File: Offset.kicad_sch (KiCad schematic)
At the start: 19 parts, among them J1 Conn_01x02, J2 Conn_01x02, J3 Conn_01x02, U1 LM358

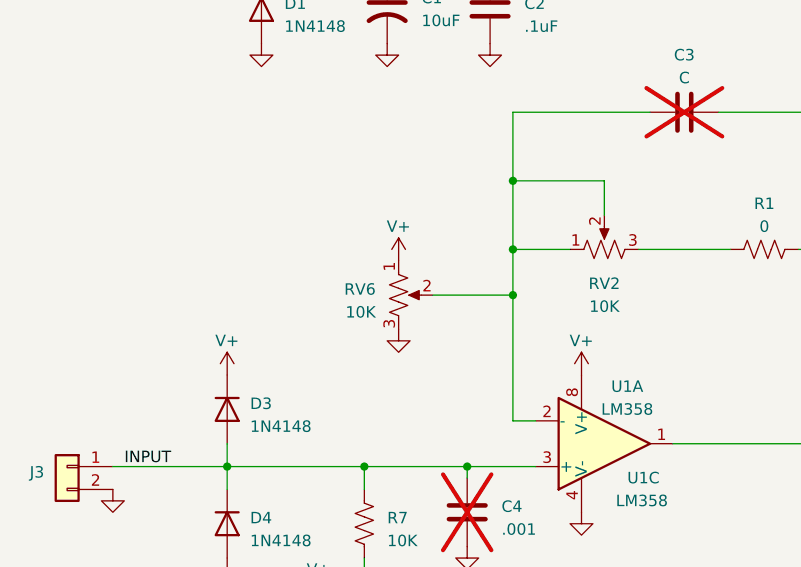
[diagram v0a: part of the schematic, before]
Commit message: Add resistor on trimmer wiper
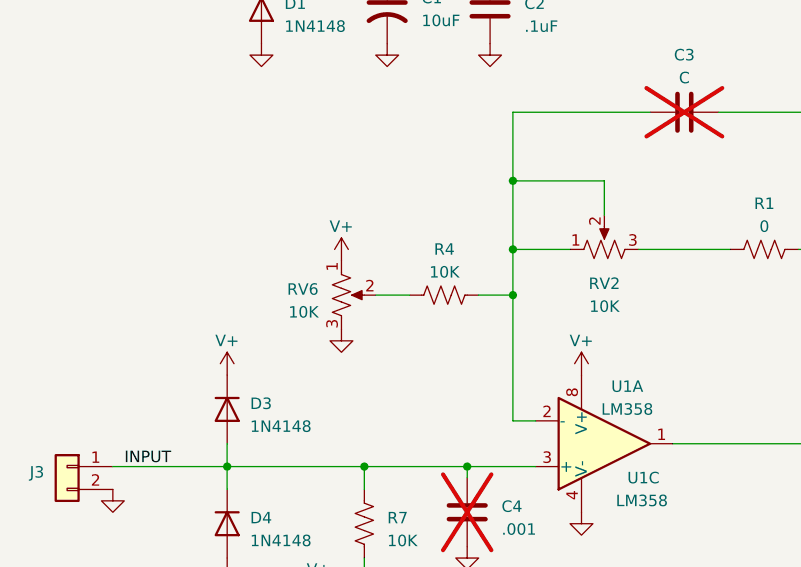
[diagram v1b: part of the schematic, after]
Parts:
- added R4: 10K, symbol Device:R_US
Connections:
- net at C3.1, RV2.1, RV2.2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: now also R4.2; no longer RV6.2
- new net: R4.1, RV6.2
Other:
- moved on the sheet: RV6
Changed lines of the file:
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@@
     (stroke (width 0) (type default))
   )
-  (wire (pts (xy 133.35 88.9) (xy 142.24 88.9))
+  (wire (pts (xy 127 88.9) (xy 130.81 88.9))
     (stroke (width 0) (type default))
   )
@@
   )
   (wire (pts (xy 156.21 83.82) (xy 166.37 83.82))
+    (stroke (width 0) (type default))
+  )
+  (wire (pts (xy 138.43 88.9) (xy 142.24 88.9))
     (stroke (width 0) (type default))
   )
@@
     )
   )
+  (symbol (lib_id "Device:R_US") (at 134.62 88.9 90) (unit 1)
+    (in_bom yes) (on_board yes) (dnp no) (fields_autoplaced)
+    (property "Reference" "R4" (at 134.62 83.82 90)
+      (effects (font (size 1.27 1.27)))
+    )
+    (property "Value" "10K" (at 134.62 86.36 90)
+      (effects (font (size 1.27 1.27)))
+    )
+    (property "Footprint" "" (at 134.874 87.884 90)
+      (effects (font (size 1.27 1.27)) hide)
+    )
+    (property "Datasheet" "~" (at 134.62 88.9 0)
+      (effects (font (size 1.27 1.27)) hide)
+    )
+    (pin "1")
+    (pin "2")
+    (instances
+      (project "Offset"
+        (path "/b9c335b0-b204-4837-ad88-f803b4ac701f"
+          (reference "R4") (unit 1)
+        )
+      )
+    )
+  )
   (symbol (lib_id "Connector_Generic:Conn_01x02") (at 198.12 105.41 0) (unit 1)
     (in_bom yes) (on_board yes) (dnp no) (fields_autoplaced)
@@
     )
   )
-  (symbol (lib_id "power:VCC") (at 129.54 85.09 0) (unit 1)
-    (in_bom yes) (on_board yes) (dnp no) (fields_autoplaced)
-    (property "Reference" "#PWR016" (at 129.54 88.9 0)
-      (effects (font (size 1.27 1.27)) hide)
-    )
-    (property "Value" "V+" (at 129.54 81.28 0)
-      (effects (font (size 1.27 1.27)))
-    )
-    (property "Footprint" "" (at 129.54 85.09 0)
-      (effects (font (size 1.27 1.27)) hide)
-    )
-    (property "Datasheet" "" (at 129.54 85.09 0)
+  (symbol (lib_id "power:VCC") (at 123.19 85.09 0) (unit 1)
+    (in_bom yes) (on_board yes) (dnp no) (fields_autoplaced)
+    (property "Reference" "#PWR016" (at 123.19 88.9 0)
+      (effects (font (size 1.27 1.27)) hide)
+    )
+    (property "Value" "V+" (at 123.19 81.28 0)
+      (effects (font (size 1.27 1.27)))
+    )
+    (property "Footprint" "" (at 123.19 85.09 0)
+      (effects (font (size 1.27 1.27)) hide)
+    )
+    (property "Datasheet" "" (at 123.19 85.09 0)
       (effects (font (size 1.27 1.27)) hide)
     )
@@
     )
   )
-  (symbol (lib_id "Device:R_Potentiometer_US") (at 129.54 88.9 0) (unit 1)
-    (in_bom yes) (on_board yes) (dnp no) (fields_autoplaced)
-    (property "Reference" "RV6" (at 127 88.265 0)
+  (symbol (lib_id "Device:R_Potentiometer_US") (at 123.19 88.9 0) (unit 1)
+    (in_bom yes) (on_board yes) (dnp no) (fields_autoplaced)
+    (property "Reference" "RV6" (at 120.65 88.265 0)
       (effects (font (size 1.27 1.27)) (justify right))
     )
-    (property "Value" "10K" (at 127 90.805 0)
+    (property "Value" "10K" (at 120.65 90.805 0)
       (effects (font (size 1.27 1.27)) (justify right))
     )
-    (property "Footprint" "" (at 129.54 88.9 0)
-      (effects (font (size 1.27 1.27)) hide)
-    )
-    (property "Datasheet" "~" (at 129.54 88.9 0)
-      (effects (font (size 1.27 1.27)) hide)
-    )
-    (property "Sim.Device" "SPICE" (at 129.54 88.9 0)
-      (effects (font (size 1.27 1.27)) hide)
-    )
-    (property "Sim.Params" "type=\"X\" model=\"RPOT value=10K ratio=0.5\" lib=RPOT_subckt.lib" (at 129.54 88.9 0)
+    (property "Footprint" "" (at 123.19 88.9 0)
+      (effects (font (size 1.27 1.27)) hide)
+    )
+    (property "Datasheet" "~" (at 123.19 88.9 0)
+      (effects (font (size 1.27 1.27)) hide)
+    )
+    (property "Sim.Device" "SPICE" (at 123.19 88.9 0)
+      (effects (font (size 1.27 1.27)) hide)
+    )
+    (property "Sim.Params" "type=\"X\" model=\"RPOT value=10K ratio=0.6\" lib=RPOT_subckt.lib" (at 123.19 88.9 0)
       (effects (font (size 1.27 1.27)) hide)
     )
@@
     )
   )
-  (symbol (lib_id "power:GND") (at 129.54 92.71 0) (unit 1)
-    (in_bom yes) (on_board yes) (dnp no) (fields_autoplaced)
-    (property "Reference" "#PWR017" (at 129.54 99.06 0)
-      (effects (font (size 1.27 1.27)) hide)
-    )
-    (property "Value" "GND" (at 129.54 97.79 0)
-      (effects (font (size 1.27 1.27)) hide)
-    )
-    (property "Footprint" "" (at 129.54 92.71 0)
-      (effects (font (size 1.27 1.27)) hide)
-    )
-    (property "Datasheet" "" (at 129.54 92.71 0)
-      (effects (font (size 1.27 1.27)) hide)
-    )
+  (symbol (lib_id "power:GND") (at 123.19 92.71 0) (unit 1)
+    (in_bom yes) (on_board yes) (dnp no) (fields_autoplaced)
+    (property "Reference" "#PWR017" (at 123.19 99.06 0)
+      (effects (font (size 1.27 1.27)) hide)
+    )
+    (property "Value" "GND" (at 123.19 97.79 0)
+      (effects (font (size 1.27 1.27)) hide)
+    )
+    (property "Footprint" "" (at 123.19 92.71 0)
+      (effects (font (size 1.27 1.27)) hide)
+    )
+    (property "Datasheet" "" (at 123.19 92.71 0)
+      (effects (font (size 1.27 1.27)) hide)
+    )

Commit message: Tweak values
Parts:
- removed RV8: 10K, symbol Device:R_Potentiometer_US
- added V2: 0.04, symbol Simulation_SPICE:VDC
- V1: value 15 -> 5
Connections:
- net GND: now also V2.2
- net at R7.1: now also V2.1
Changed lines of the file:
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@@
-    (stroke (width 0) (type default))
-  )
-  (wire (pts (xy 130.81 124.46) (xy 130.81 125.73))
-    (stroke (width 0) (type default))
-  )
-  (wire (pts (xy 129.54 124.46) (xy 130.81 124.46))
     (stroke (width 0) (type default))
   )
@@
     (stroke (width 0) (type default))
   )
-  (wire (pts (xy 125.73 118.11) (xy 125.73 120.65))
+  (wire (pts (xy 125.73 118.11) (xy 125.73 121.92))
     (stroke (width 0) (type default))
   )
@@
     (stroke (width 0) (type default))
   )
-  (wire (pts (xy 120.65 124.46) (xy 120.65 123.19))
-    (stroke (width 0) (type default))
-  )
   (wire (pts (xy 152.4 76.2) (xy 152.4 80.01))
     (stroke (width 0) (type default))
@@
   )
   (wire (pts (xy 110.49 105.41) (xy 110.49 107.95))
-    (stroke (width 0) (type default))
-  )
-  (wire (pts (xy 121.92 124.46) (xy 120.65 124.46))
     (stroke (width 0) (type default))
   )
@@
       (effects (font (size 1.27 1.27)) hide)
     )
-    (property "Sim.Params" "type=\"X\" model=\"RPOT value=10K ratio=0.6\" lib=RPOT_subckt.lib" (at 123.19 88.9 0)
+    (property "Sim.Params" "type=\"X\" model=\"RPOT value=10K ratio=0.9\" lib=RPOT_subckt.lib" (at 123.19 88.9 0)
       (effects (font (size 1.27 1.27)) hide)
     )
@@
     )
   )
-  (symbol (lib_id "Device:R_Potentiometer_US") (at 125.73 124.46 90) (unit 1)
-    (in_bom yes) (on_board yes) (dnp no) (fields_autoplaced)
-    (property "Reference" "RV8" (at 125.73 128.27 90)
-      (effects (font (size 1.27 1.27)))
-    )
-    (property "Value" "10K" (at 125.73 130.81 90)
-      (effects (font (size 1.27 1.27)))
-    )
-    (property "Footprint" "" (at 125.73 124.46 0)
-      (effects (font (size 1.27 1.27)) hide)
-    )
-    (property "Datasheet" "~" (at 125.73 124.46 0)
-      (effects (font (size 1.27 1.27)) hide)
-    )
-    (property "Sim.Device" "SPICE" (at 125.73 124.46 0)
-      (effects (font (size 1.27 1.27)) hide)
-    )
-    (property "Sim.Params" "type=\"X\" model=\"RPOT value=10K ratio=0.5\" lib=RPOT_subckt.lib" (at 125.73 124.46 0)
-      (effects (font (size 1.27 1.27)) hide)
-    )
-    (pin "1")
-    (pin "2")
-    (pin "3")
-    (instances
-      (project "Offset"
-        (path "/b9c335b0-b204-4837-ad88-f803b4ac701f"
-          (reference "RV8") (unit 1)
-        )
-      )
-    )
-  )
   (symbol (lib_id "power:GND") (at 110.49 118.11 0) (unit 1)
     (in_bom yes) (on_board yes) (dnp no) (fields_autoplaced)
@@
     )
   )
-  (symbol (lib_id "power:VCC") (at 120.65 123.19 0) (unit 1)
-    (in_bom yes) (on_board yes) (dnp no) (fields_autoplaced)
-    (property "Reference" "#PWR011" (at 120.65 127 0)
-      (effects (font (size 1.27 1.27)) hide)
-    )
-    (property "Value" "V+" (at 120.65 119.38 0)
-      (effects (font (size 1.27 1.27)))
-    )
-    (property "Footprint" "" (at 120.65 123.19 0)
-      (effects (font (size 1.27 1.27)) hide)
-    )
-    (property "Datasheet" "" (at 120.65 123.19 0)
-      (effects (font (size 1.27 1.27)) hide)
-    )
-    (pin "1")
-    (instances
-      (project "Offset"
-        (path "/b9c335b0-b204-4837-ad88-f803b4ac701f"
-          (reference "#PWR011") (unit 1)
-        )
-      )
-    )
-  )
   (symbol (lib_id "Device:C_Polarized_US") (at 128.27 57.15 0) (unit 1)
     (in_bom yes) (on_board yes) (dnp no) (fields_autoplaced)
@@
         (path "/b9c335b0-b204-4837-ad88-f803b4ac701f"
           (reference "#PWR018") (unit 1)
+        )
+      )
+    )
+  )
+  (symbol (lib_id "Simulation_SPICE:VDC") (at 125.73 127 0) (unit 1)
+    (in_bom yes) (on_board yes) (dnp no) (fields_autoplaced)
+    (property "Reference" "V2" (at 129.54 126.3292 0)
+      (effects (font (size 1.27 1.27)) (justify left))
+    )
+    (property "Value" "0.04" (at 129.54 128.8692 0)
+      (effects (font (size 1.27 1.27)) (justify left))
+    )
+    (property "Footprint" "" (at 125.73 127 0)
+      (effects (font (size 1.27 1.27)) hide)
+    )
+    (property "Datasheet" "~" (at 125.73 127 0)
+      (effects (font (size 1.27 1.27)) hide)
+    )
+    (property "Sim.Pins" "1=+ 2=-" (at 125.73 127 0)
+      (effects (font (size 1.27 1.27)) hide)
+    )
+    (property "Sim.Type" "DC" (at 125.73 127 0)
+      (effects (font (size 1.27 1.27)) hide)
+    )
+    (property "Sim.Device" "V" (at 125.73 127 0)
+      (effects (font (size 1.27 1.27)) (justify left) hide)
+    )
+    (pin "1")
+    (pin "2")
+    (instances
+      (project "Offset"
+        (path "/b9c335b0-b204-4837-ad88-f803b4ac701f"
+          (reference "V2") (unit 1)
         )
       )
@@
     )
   )
-  (symbol (lib_id "power:GND") (at 130.81 125.73 0) (unit 1)
-    (in_bom yes) (on_board yes) (dnp no) (fields_autoplaced)
-    (property "Reference" "#PWR010" (at 130.81 132.08 0)
-      (effects (font (size 1.27 1.27)) hide)
-    )
-    (property "Value" "GND" (at 130.81 130.81 0)
-      (effects (font (size 1.27 1.27)) hide)
-    )
-    (property "Footprint" "" (at 130.81 125.73 0)
-      (effects (font (size 1.27 1.27)) hide)
-    )
-    (property "Datasheet" "" (at 130.81 125.73 0)
+  (symbol (lib_id "power:GND") (at 125.73 132.08 0) (unit 1)
+    (in_bom yes) (on_board yes) (dnp no) (fields_autoplaced)
+    (property "Reference" "#PWR010" (at 125.73 138.43 0)
+      (effects (font (size 1.27 1.27)) hide)
+    )
+    (property "Value" "GND" (at 125.73 137.16 0)
+      (effects (font (size 1.27 1.27)) hide)
+    )
+    (property "Footprint" "" (at 125.73 132.08 0)
+      (effects (font (size 1.27 1.27)) hide)
+    )
+    (property "Datasheet" "" (at 125.73 132.08 0)
       (effects (font (size 1.27 1.27)) hide)
     )
@@
       (effects (font (size 1.27 1.27)) (justify left))
     )
-    (property "Value" "15" (at 173.99 46.3192 0)
-      (effects (font (size 1.27 1.27)) (justify left))
-    )
+    (property "Value" "5" (at 173.99 46.3192 0)
+      (effects (font (size 1.27 1.27)) (justify left))
+    )
